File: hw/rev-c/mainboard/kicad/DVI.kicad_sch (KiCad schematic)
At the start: 14 parts, among them J21 NOT_HDMI_A

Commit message: hw: update HDMI footprint
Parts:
- J21: footprint Connector_HDMI:HDMI_A_Molex_208658-1001_Horizontal -> Connector_Video:HDMI_A_Molex_208658-1001_Horizontal
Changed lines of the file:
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@@
 			)
 		)
-		(property "Footprint" "Connector_HDMI:HDMI_A_Molex_208658-1001_Horizontal"
+		(property "Footprint" "Connector_Video:HDMI_A_Molex_208658-1001_Horizontal"
 			(at 191.135 88.9 0)
 			(effects

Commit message: hw: mark pads as "heat sink" to avoid DRC error
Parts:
- J21: footprint Connector_Video:HDMI_A_Molex_208658-1001_Horizontal -> EconoPET:HDMI_A_Molex_208658-1001_Horizontal
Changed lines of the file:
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@@
 			)
 		)
-		(property "Footprint" "Connector_Video:HDMI_A_Molex_208658-1001_Horizontal"
+		(property "Footprint" "EconoPET:HDMI_A_Molex_208658-1001_Horizontal"
 			(at 191.135 88.9 0)
 			(effects

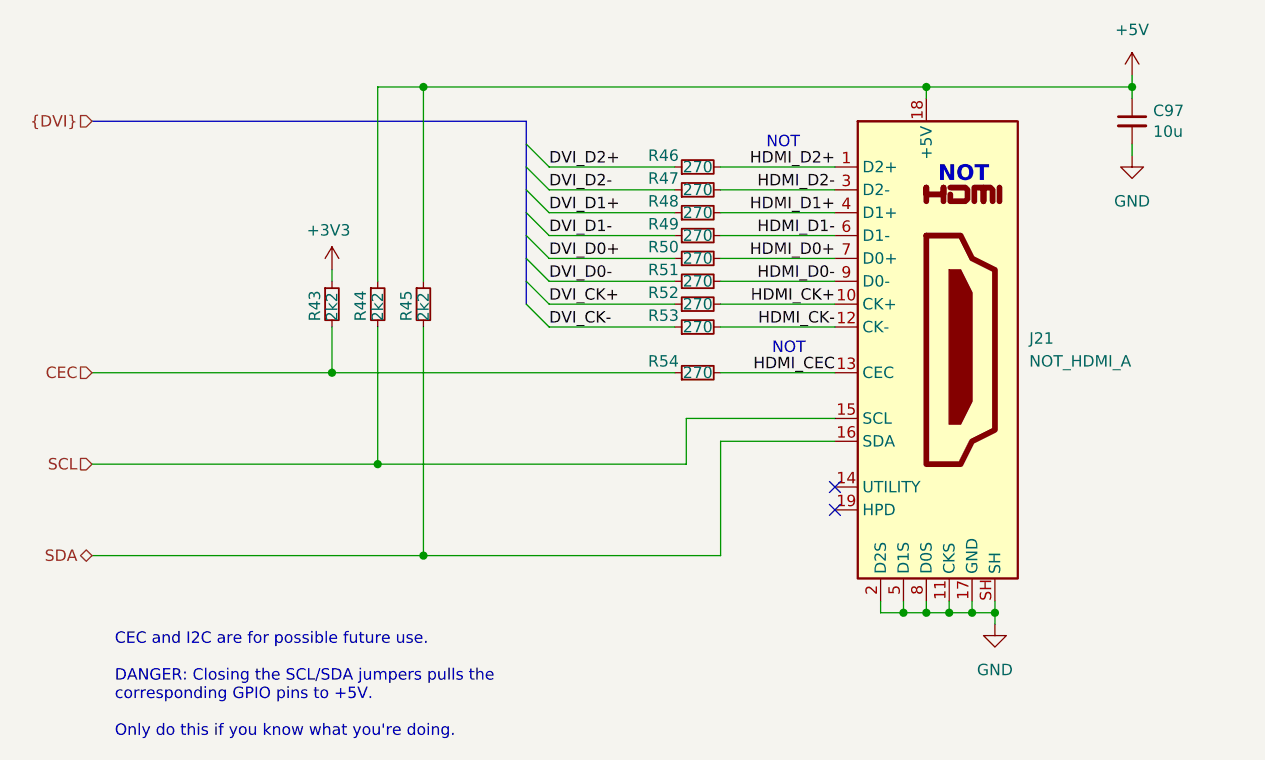
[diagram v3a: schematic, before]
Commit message: hw: renumber reference designators
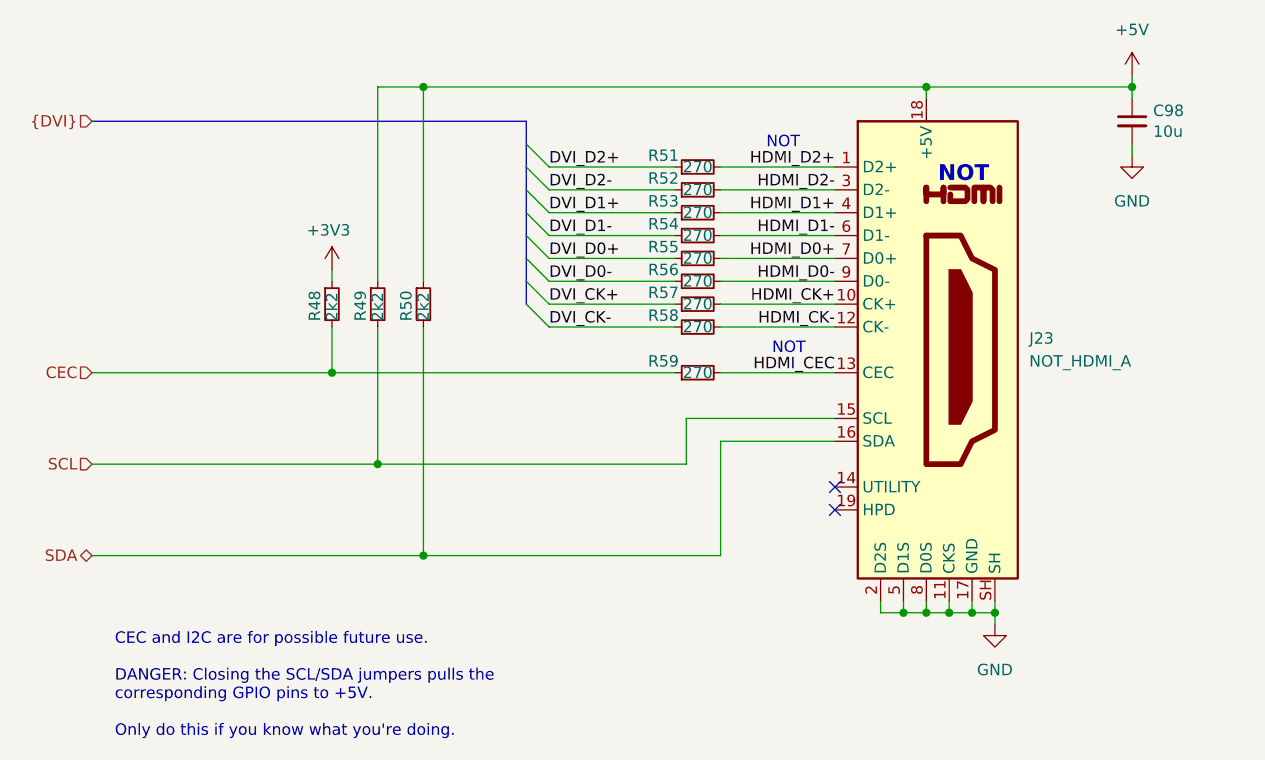
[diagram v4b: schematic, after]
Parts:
- renumbered C97 to C98, J21 to J23, R43 to R48, R44 to R49, R45 to R50, R46 to R51, R47 to R52, R48 to R53, R49 to R54, R50 to R55, R51 to R56, R52 to R57, R53 to R58, R54 to R59
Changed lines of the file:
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@@
 		(on_board yes)
 		(dnp no)
-		(property "Reference" "R52"
+		(property "Reference" "R57"
 			(at 161.29 82.55 90)
 			(effects
@@
 			(project ""
 				(path "/2eea20e6-112c-411a-b615-885ae773135a/00000000-0000-0000-0000-0000617d6918/b70241ab-8a5c-42d5-a1ab-8f4bc50a1197/c562673a-fe22-414c-81e5-6834e9fead43"
-					(reference "R52")
+					(reference "R57")
 					(unit 1)
 				)
@@
 		(on_board yes)
 		(dnp no)
-		(property "Reference" "R49"
+		(property "Reference" "R54"
 			(at 161.29 74.93 90)
 			(effects
@@
 			(project ""
 				(path "/2eea20e6-112c-411a-b615-885ae773135a/00000000-0000-0000-0000-0000617d6918/b70241ab-8a5c-42d5-a1ab-8f4bc50a1197/c562673a-fe22-414c-81e5-6834e9fead43"
-					(reference "R49")
+					(reference "R54")
 					(unit 1)
 				)
@@
 		(on_board yes)
 		(dnp no)
-		(property "Reference" "R45"
+		(property "Reference" "R50"
 			(at 132.715 85.725 90)
 			(effects
@@
 			(project ""
 				(path "/2eea20e6-112c-411a-b615-885ae773135a/00000000-0000-0000-0000-0000617d6918/b70241ab-8a5c-42d5-a1ab-8f4bc50a1197/c562673a-fe22-414c-81e5-6834e9fead43"
-					(reference "R45")
+					(reference "R50")
 					(unit 1)
 				)
@@
 		(on_board yes)
 		(dnp no)
-		(property "Reference" "R44"
+		(property "Reference" "R49"
 			(at 127.635 85.725 90)
 			(effects
@@
 			(project ""
 				(path "/2eea20e6-112c-411a-b615-885ae773135a/00000000-0000-0000-0000-0000617d6918/b70241ab-8a5c-42d5-a1ab-8f4bc50a1197/c562673a-fe22-414c-81e5-6834e9fead43"
-					(reference "R44")
+					(reference "R49")
 					(unit 1)
 				)
@@
 		(dnp no)
 		(fields_autoplaced yes)
-		(property "Reference" "#PWR0163"
+		(property "Reference" "#PWR0164"
 			(at 213.36 62.23 0)
 			(effects
@@
 			(project ""
 				(path "/2eea20e6-112c-411a-b615-885ae773135a/00000000-0000-0000-0000-0000617d6918/b70241ab-8a5c-42d5-a1ab-8f4bc50a1197/c562673a-fe22-414c-81e5-6834e9fead43"
-					(reference "#PWR0163")
+					(reference "#PWR0164")
 					(unit 1)
 				)
@@
 		(on_board yes)
 		(dnp no)
-		(property "Reference" "#PWR0161"
+		(property "Reference" "#PWR0162"
 			(at 124.46 83.82 0)
 			(effects
@@
 			(project ""
 				(path "/2eea20e6-112c-411a-b615-885ae773135a/00000000-0000-0000-0000-0000617d6918/b70241ab-8a5c-42d5-a1ab-8f4bc50a1197/c562673a-fe22-414c-81e5-6834e9fead43"
-					(reference "#PWR0161")
+					(reference "#PWR0162")
 					(unit 1)
 				)
@@
 		(on_board yes)
 		(dnp no)
-		(property "Reference" "J21"
+		(property "Reference" "J23"
 			(at 201.93 87.63 0)
 			(effects
@@
 			(project ""
 				(path "/2eea20e6-112c-411a-b615-885ae773135a/00000000-0000-0000-0000-0000617d6918/b70241ab-8a5c-42d5-a1ab-8f4bc50a1197/c562673a-fe22-414c-81e5-6834e9fead43"
-					(reference "J21")
+					(reference "J23")
 					(unit 1)
 				)
@@
 		(on_board yes)
 		(dnp no)
-		(property "Reference" "R46"
+		(property "Reference" "R51"
 			(at 161.29 67.31 90)
 			(effects
@@
 			(project ""
 				(path "/2eea20e6-112c-411a-b615-885ae773135a/00000000-0000-0000-0000-0000617d6918/b70241ab-8a5c-42d5-a1ab-8f4bc50a1197/c562673a-fe22-414c-81e5-6834e9fead43"
-					(reference "R46")
+					(reference "R51")
 					(unit 1)
 				)
@@
 		(on_board yes)
 		(dnp no)
-		(property "Reference" "R54"
+		(property "Reference" "R59"
 			(at 161.29 90.17 90)
 			(effects
@@
 			(project ""
 				(path "/2eea20e6-112c-411a-b615-885ae773135a/00000000-0000-0000-0000-0000617d6918/b70241ab-8a5c-42d5-a1ab-8f4bc50a1197/c562673a-fe22-414c-81e5-6834e9fead43"
-					(reference "R54")
+					(reference "R59")
 					(unit 1)
 				)
@@
 		(on_board yes)
 		(dnp no)
-		(property "Reference" "R51"
+		(property "Reference" "R56"
 			(at 161.29 80.01 90)
 			(effects
@@
 			(project ""
 				(path "/2eea20e6-112c-411a-b615-885ae773135a/00000000-0000-0000-0000-0000617d6918/b70241ab-8a5c-42d5-a1ab-8f4bc50a1197/c562673a-fe22-414c-81e5-6834e9fead43"
-					(reference "R51")
+					(reference "R56")
 					(unit 1)
 				)
@@
 		(on_board yes)
 		(dnp no)
-		(property "Reference" "R53"
+		(property "Reference" "R58"
 			(at 161.29 85.09 90)
 			(effects
@@
 			(project ""
 				(path "/2eea20e6-112c-411a-b615-885ae773135a/00000000-0000-0000-0000-0000617d6918/b70241ab-8a5c-42d5-a1ab-8f4bc50a1197/c562673a-fe22-414c-81e5-6834e9fead43"
-					(reference "R53")
+					(reference "R58")
 					(unit 1)
 				)
@@
 		(on_board yes)
 		(dnp no)
-		(property "Reference" "C97"
+		(property "Reference" "C98"
 			(at 215.6968 62.3316 0)
 			(effects
@@
 			(project ""
 				(path "/2eea20e6-112c-411a-b615-885ae773135a/00000000-0000-0000-0000-0000617d6918/b70241ab-8a5c-42d5-a1ab-8f4bc50a1197/c562673a-fe22-414c-81e5-6834e9fead43"
-					(reference "C97")
+					(reference "C98")
 					(unit 1)
 				)
@@
 		(on_board yes)
 		(dnp no)
-		(property "Reference" "R50"
+		(property "Reference" "R55"
 			(at 161.29 77.47 90)
 			(effects
@@
 			(project ""
 				(path "/2eea20e6-112c-411a-b615-885ae773135a/00000000-0000-0000-0000-0000617d6918/b70241ab-8a5c-42d5-a1ab-8f4bc50a1197/c562673a-fe22-414c-81e5-6834e9fead43"
-					(reference "R50")
+					(reference "R55")
 					(unit 1)
 				)
@@
 		(on_board yes)
 		(dnp no)
-		(property "Reference" "R43"
+		(property "Reference" "R48"
 			(at 122.555 85.725 90)
 			(effects
@@
 			(project ""
 				(path "/2eea20e6-112c-411a-b615-885ae773135a/00000000-0000-0000-0000-0000617d6918/b70241ab-8a5c-42d5-a1ab-8f4bc50a1197/c562673a-fe22-414c-81e5-6834e9fead43"
-					(reference "R43")
+					(reference "R48")
 					(unit 1)
 				)
@@
 		(dnp no)
 		(fields_autoplaced yes)
-		(property "Reference" "#PWR0162"
+		(property "Reference" "#PWR0163"
 			(at 198.12 125.73 0)
 			(effects
@@
 			(project ""
 				(path "/2eea20e6-112c-411a-b615-885ae773135a/00000000-0000-0000-0000-0000617d6918/b70241ab-8a5c-42d5-a1ab-8f4bc50a1197/c562673a-fe22-414c-81e5-6834e9fead43"
-					(reference "#PWR0162")
+					(reference "#PWR0163")
 					(unit 1)
 				)
@@
 		(on_board yes)
 		(dnp no)
-		(property "Reference" "R47"
+		(property "Reference" "R52"
 			(at 161.29 69.85 90)
 			(effects
@@
 			(project ""
 				(path "/2eea20e6-112c-411a-b615-885ae773135a/00000000-0000-0000-0000-0000617d6918/b70241ab-8a5c-42d5-a1ab-8f4bc50a1197/c562673a-fe22-414c-81e5-6834e9fead43"
-					(reference "R47")
+					(reference "R52")
 					(unit 1)
 				)
@@
 		(on_board yes)
 		(dnp no)
-		(property "Reference" "R48"
+		(property "Reference" "R53"
 			(at 161.29 72.39 90)
 			(effects
@@
 			(project ""
 				(path "/2eea20e6-112c-411a-b615-885ae773135a/00000000-0000-0000-0000-0000617d6918/b70241ab-8a5c-42d5-a1ab-8f4bc50a1197/c562673a-fe22-414c-81e5-6834e9fead43"
-					(reference "R48")
+					(reference "R53")
 					(unit 1)
 				)
@@
 		(dnp no)
 		(fields_autoplaced yes)
-		(property "Reference" "#PWR0164"
+		(property "Reference" "#PWR0165"
 			(at 213.36 73.66 0)
 			(effects
@@
 			(project ""
 				(path "/2eea20e6-112c-411a-b615-885ae773135a/00000000-0000-0000-0000-0000617d6918/b70241ab-8a5c-42d5-a1ab-8f4bc50a1197/c562673a-fe22-414c-81e5-6834e9fead43"
-					(reference "#PWR0164")
-					(unit 1)
-				)
+					(reference "#PWR0165")
+					(unit 1)
+				)

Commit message: hw: match original PET designators for connectors
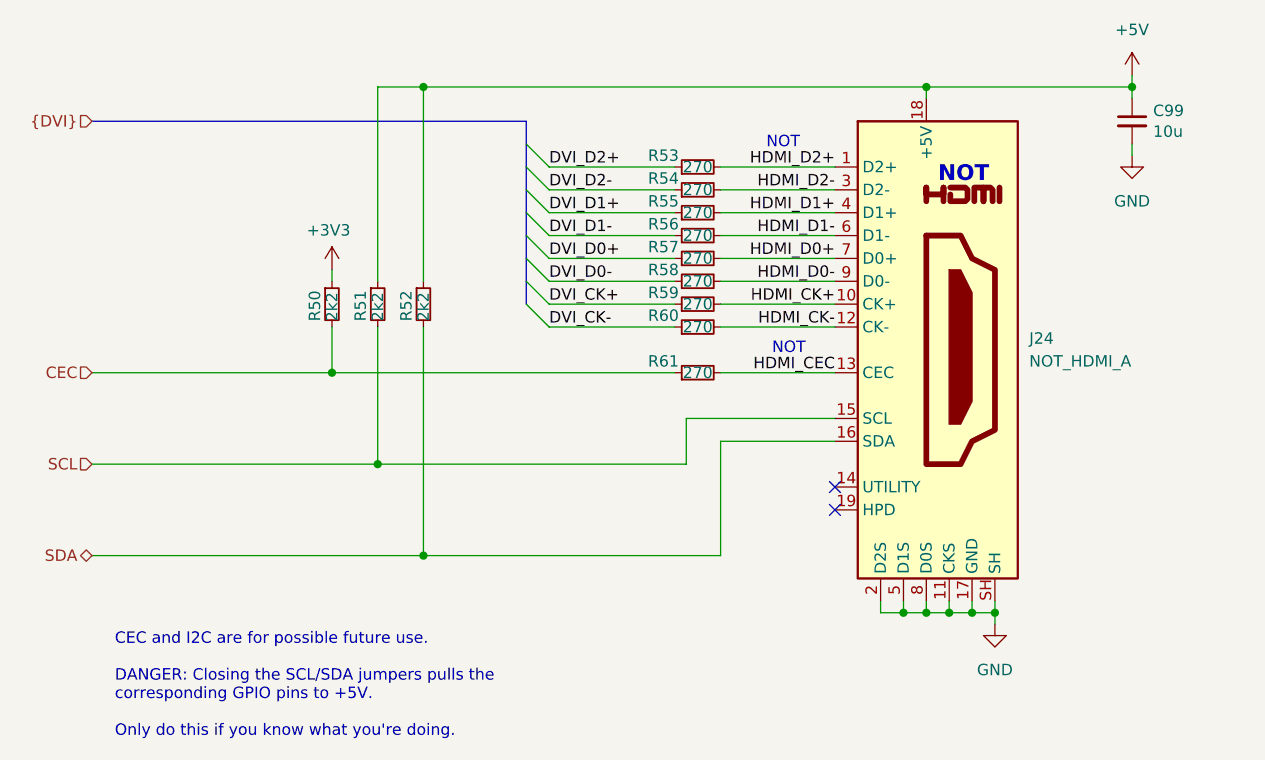
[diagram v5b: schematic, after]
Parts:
- renumbered C98 to C99, J23 to J24, R48 to R50, R49 to R51, R50 to R52, R51 to R53, R52 to R54, R53 to R55, R54 to R56, R55 to R57, R56 to R58, R57 to R59, R58 to R60, R59 to R61
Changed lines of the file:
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@@
 		(on_board yes)
 		(dnp no)
-		(property "Reference" "R57"
+		(property "Reference" "R59"
 			(at 161.29 82.55 90)
 			(effects
@@
 			(project ""
 				(path "/2eea20e6-112c-411a-b615-885ae773135a/00000000-0000-0000-0000-0000617d6918/b70241ab-8a5c-42d5-a1ab-8f4bc50a1197/c562673a-fe22-414c-81e5-6834e9fead43"
-					(reference "R57")
+					(reference "R59")
 					(unit 1)
 				)
@@
 		(on_board yes)
 		(dnp no)
-		(property "Reference" "R54"
+		(property "Reference" "R56"
 			(at 161.29 74.93 90)
 			(effects
@@
 			(project ""
 				(path "/2eea20e6-112c-411a-b615-885ae773135a/00000000-0000-0000-0000-0000617d6918/b70241ab-8a5c-42d5-a1ab-8f4bc50a1197/c562673a-fe22-414c-81e5-6834e9fead43"
-					(reference "R54")
+					(reference "R56")
 					(unit 1)
 				)
@@
 		(on_board yes)
 		(dnp no)
-		(property "Reference" "R50"
+		(property "Reference" "R52"
 			(at 132.715 85.725 90)
 			(effects
@@
 			(project ""
 				(path "/2eea20e6-112c-411a-b615-885ae773135a/00000000-0000-0000-0000-0000617d6918/b70241ab-8a5c-42d5-a1ab-8f4bc50a1197/c562673a-fe22-414c-81e5-6834e9fead43"
-					(reference "R50")
+					(reference "R52")
 					(unit 1)
 				)
@@
 		(on_board yes)
 		(dnp no)
-		(property "Reference" "R49"
+		(property "Reference" "R51"
 			(at 127.635 85.725 90)
 			(effects
@@
 			(project ""
 				(path "/2eea20e6-112c-411a-b615-885ae773135a/00000000-0000-0000-0000-0000617d6918/b70241ab-8a5c-42d5-a1ab-8f4bc50a1197/c562673a-fe22-414c-81e5-6834e9fead43"
-					(reference "R49")
+					(reference "R51")
 					(unit 1)
 				)
@@
 		(on_board yes)
 		(dnp no)
-		(property "Reference" "J23"
+		(property "Reference" "J24"
 			(at 201.93 87.63 0)
 			(effects
@@
 			(project ""
 				(path "/2eea20e6-112c-411a-b615-885ae773135a/00000000-0000-0000-0000-0000617d6918/b70241ab-8a5c-42d5-a1ab-8f4bc50a1197/c562673a-fe22-414c-81e5-6834e9fead43"
-					(reference "J23")
+					(reference "J24")
 					(unit 1)
 				)
@@
 		(on_board yes)
 		(dnp no)
-		(property "Reference" "R51"
+		(property "Reference" "R53"
 			(at 161.29 67.31 90)
 			(effects
@@
 			(project ""
 				(path "/2eea20e6-112c-411a-b615-885ae773135a/00000000-0000-0000-0000-0000617d6918/b70241ab-8a5c-42d5-a1ab-8f4bc50a1197/c562673a-fe22-414c-81e5-6834e9fead43"
-					(reference "R51")
+					(reference "R53")
 					(unit 1)
 				)
@@
 		(on_board yes)
 		(dnp no)
-		(property "Reference" "R59"
+		(property "Reference" "R61"
 			(at 161.29 90.17 90)
 			(effects
@@
 			(project ""
 				(path "/2eea20e6-112c-411a-b615-885ae773135a/00000000-0000-0000-0000-0000617d6918/b70241ab-8a5c-42d5-a1ab-8f4bc50a1197/c562673a-fe22-414c-81e5-6834e9fead43"
-					(reference "R59")
+					(reference "R61")
 					(unit 1)
 				)
@@
 		(on_board yes)
 		(dnp no)
-		(property "Reference" "R56"
+		(property "Reference" "R58"
 			(at 161.29 80.01 90)
 			(effects
@@
 			(project ""
 				(path "/2eea20e6-112c-411a-b615-885ae773135a/00000000-0000-0000-0000-0000617d6918/b70241ab-8a5c-42d5-a1ab-8f4bc50a1197/c562673a-fe22-414c-81e5-6834e9fead43"
-					(reference "R56")
+					(reference "R58")
 					(unit 1)
 				)
@@
 		(on_board yes)
 		(dnp no)
-		(property "Reference" "R58"
+		(property "Reference" "R60"
 			(at 161.29 85.09 90)
 			(effects
@@
 			(project ""
 				(path "/2eea20e6-112c-411a-b615-885ae773135a/00000000-0000-0000-0000-0000617d6918/b70241ab-8a5c-42d5-a1ab-8f4bc50a1197/c562673a-fe22-414c-81e5-6834e9fead43"
-					(reference "R58")
+					(reference "R60")
 					(unit 1)
 				)
@@
 		(on_board yes)
 		(dnp no)
-		(property "Reference" "C98"
+		(property "Reference" "C99"
 			(at 215.6968 62.3316 0)
 			(effects
@@
 			(project ""
 				(path "/2eea20e6-112c-411a-b615-885ae773135a/00000000-0000-0000-0000-0000617d6918/b70241ab-8a5c-42d5-a1ab-8f4bc50a1197/c562673a-fe22-414c-81e5-6834e9fead43"
-					(reference "C98")
+					(reference "C99")
 					(unit 1)
 				)
@@
 		(on_board yes)
 		(dnp no)
-		(property "Reference" "R55"
+		(property "Reference" "R57"
 			(at 161.29 77.47 90)
 			(effects
@@
 			(project ""
 				(path "/2eea20e6-112c-411a-b615-885ae773135a/00000000-0000-0000-0000-0000617d6918/b70241ab-8a5c-42d5-a1ab-8f4bc50a1197/c562673a-fe22-414c-81e5-6834e9fead43"
-					(reference "R55")
+					(reference "R57")
 					(unit 1)
 				)
@@
 		(on_board yes)
 		(dnp no)
-		(property "Reference" "R48"
+		(property "Reference" "R50"
 			(at 122.555 85.725 90)
 			(effects
@@
 			(project ""
 				(path "/2eea20e6-112c-411a-b615-885ae773135a/00000000-0000-0000-0000-0000617d6918/b70241ab-8a5c-42d5-a1ab-8f4bc50a1197/c562673a-fe22-414c-81e5-6834e9fead43"
-					(reference "R48")
+					(reference "R50")
 					(unit 1)
 				)
@@
 		(on_board yes)
 		(dnp no)
-		(property "Reference" "R52"
+		(property "Reference" "R54"
 			(at 161.29 69.85 90)
 			(effects
@@
 			(project ""
 				(path "/2eea20e6-112c-411a-b615-885ae773135a/00000000-0000-0000-0000-0000617d6918/b70241ab-8a5c-42d5-a1ab-8f4bc50a1197/c562673a-fe22-414c-81e5-6834e9fead43"
-					(reference "R52")
+					(reference "R54")
 					(unit 1)
 				)
@@
 		(on_board yes)
 		(dnp no)
-		(property "Reference" "R53"
+		(property "Reference" "R55"
 			(at 161.29 72.39 90)
 			(effects
@@
 			(project ""
 				(path "/2eea20e6-112c-411a-b615-885ae773135a/00000000-0000-0000-0000-0000617d6918/b70241ab-8a5c-42d5-a1ab-8f4bc50a1197/c562673a-fe22-414c-81e5-6834e9fead43"
-					(reference "R53")
-					(unit 1)
-				)
+					(reference "R55")
+					(unit 1)
+				)

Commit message: hw: perimeter stitching (wip)
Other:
- note added: "CEC and I2C are for possible future use. DANGER: Closing the SCL/SDA jumpers pulls the corresponding RP2040 GPIO pins to +5V. Only do this if you know what you're doing."
- note removed: "CEC and I2C are for possible future use. DANGER: Closing the SCL/SDA jumpers pulls the corresponding GPIO pins to +5V. Only do this if you know what you're doing."
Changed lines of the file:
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@@
 		)
 	)
-	(text "CEC and I2C are for possible future use.\n\nDANGER: Closing the SCL/SDA jumpers pulls the\ncorresponding GPIO pins to +5V.\n\nOnly do this if you know what you're doing."
+	(text "CEC and I2C are for possible future use.\n\nDANGER: Closing the SCL/SDA jumpers pulls the\ncorresponding RP2040 GPIO pins to +5V.\n\nOnly do this if you know what you're doing."
 		(exclude_from_sim no)
 		(at 100.33 132.08 0)
